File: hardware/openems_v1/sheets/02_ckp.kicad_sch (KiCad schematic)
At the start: 0 parts

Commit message: feat(hw): fecha esquemático v2 — sheets 01/02/03/05/07/11 desenhadas, ERC 0
- 01_power: nova — P-FET reverse (Q1) + F1 30A + SMBJ24CA + bulk 100µF/100nF,
  star GND (PGND/SGND/AGND) via PWR_FLAG na sheet produtora, VBAT limpo para
  o resto da placa (buck/LDO ficam no TPS65381A, sheet PMIC)
- 02_ckp / 03_cmp: CKP Hall (espelho do CMP) → MCU.PA0/PA1
- 05_analog: refeita do zero a partir do pinout_v2 (13 canais ADC), mapa
  pré-v2 descartado
- 11_mcu_h562: netlist U1 corrigido (lib_id não resolvia pinos — 100 pinos
  caíam na mesma net); globals PA0/PA1/PB4 sincronizados com as sheets acima
- 07_flex: pino corrigido para PB4 (pinout_v2)
- READMEs (hardware/openems_v1, docs/hw/schematic) actualizados ao estado
  real por sheet

Passos 1-5 do roadmap do esquemático fechados; ERC isolado por sheet em 0
erros (avisos residuais são globals sem sheet destino ainda — esperado).

Co-Authored-By: Claude Sonnet 5 <noreply@anthropic.com>
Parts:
- added C2: 330pF, Capacitor_SMD:C_0603_1608Metric, symbol Device:C
- added D2: 3V3 unidirectional, Diode_SMD:D_SOD-123, symbol Device:D_TVS
- added R10, R11: 10k, Resistor_SMD:R_0603_1608Metric, symbol Device:R
- added R12: 15k, Resistor_SMD:R_0603_1608Metric, symbol Device:R
- added R13: 330, Resistor_SMD:R_0603_1608Metric, symbol Device:R
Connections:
- new net +5V_SENS_A: R10.1
- new net AGND: C2.2, D2.2 (A2)
- new net J1.CKP_SIG: D2.1 (A1), R10.2, R11.1
- new net MCU.PA0: C2.1, R13.2
- new net N_CKP_DIV: R11.2, R12.1, R13.1
- new net SGND: R12.2
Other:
- note added: "Sheet 02 — CKP Hall (60-2) → MCU.PA0 | mirror of 03_cmp"

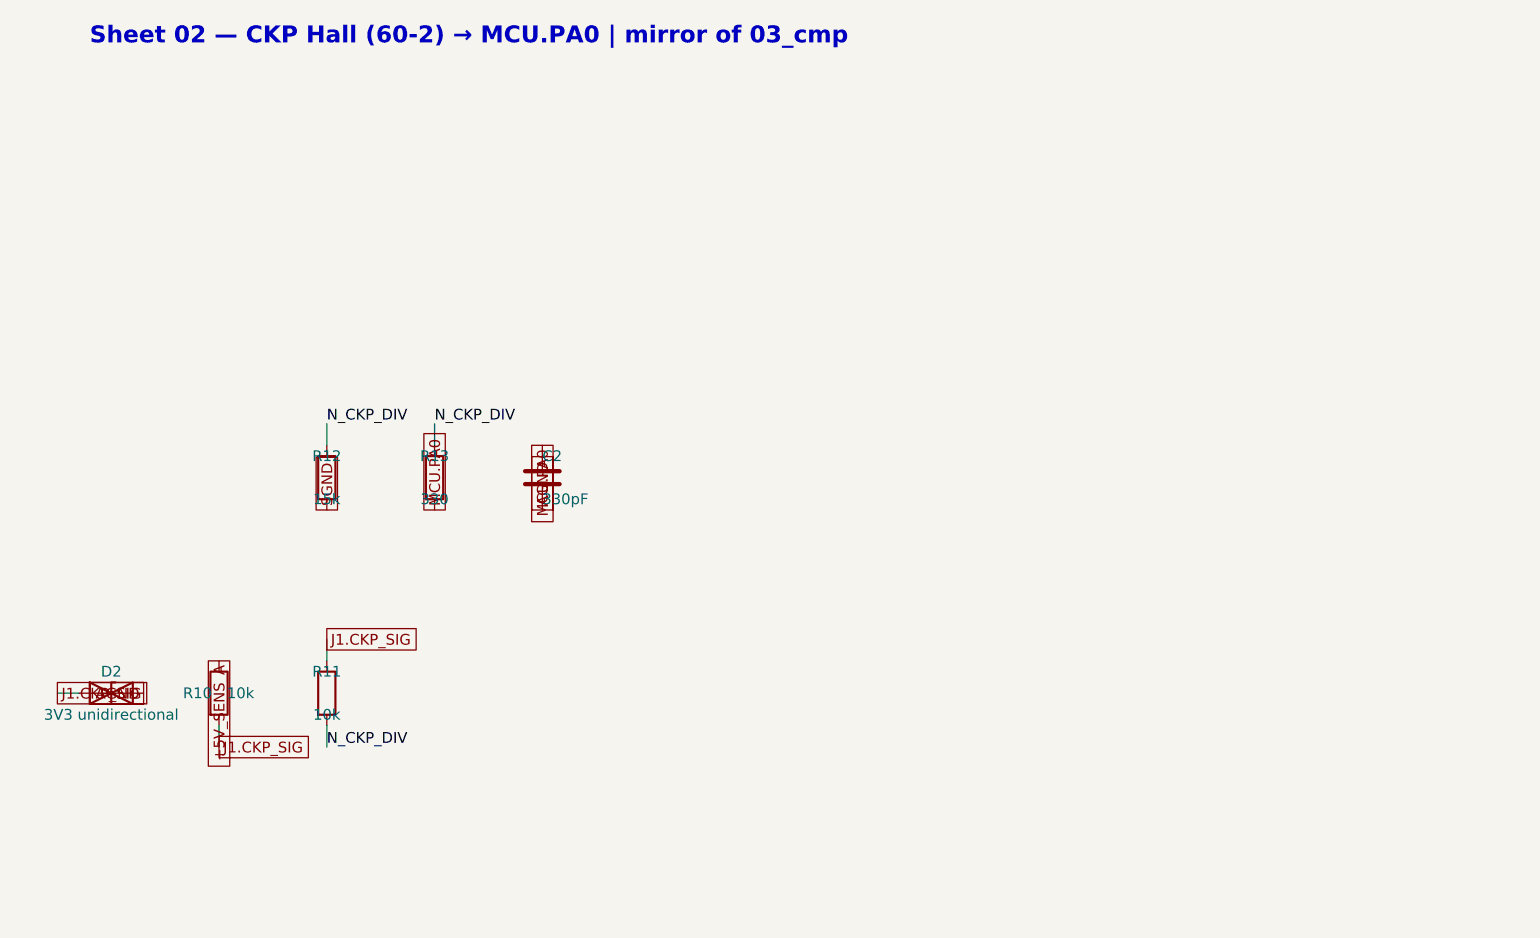
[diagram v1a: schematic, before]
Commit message: fix(hw): corrige legibilidade de 01_power e 02_ckp — layout, não topologia
Render visual (kicad-cli export svg) mostrou os componentes sobrepostos uns
aos outros (D1/C1/C2 e R10/D2 amontoados no canto da folha) apesar do ERC
0 erros — ERC não valida legibilidade, só conectividade. Nenhum bloco
tinha sido efectivamente olhado desde que foi desenhado.

- Pitch entre componentes alargado (10-15mm → 20-35mm)
- Valores do Value field encurtados (o detalhe fica na doc, não no canvas)
- Orientação dos labels ajustada para apontar para fora do corpo do
  símbolo em vez de atravessá-lo (Q1 gate, D1/D2 TVS, C2)
- Conectividade eléctrica idêntica à anterior — só reposicionamento;
  ERC 0 erros mantido nas duas sheets

Co-Authored-By: Claude Sonnet 5 <noreply@anthropic.com>
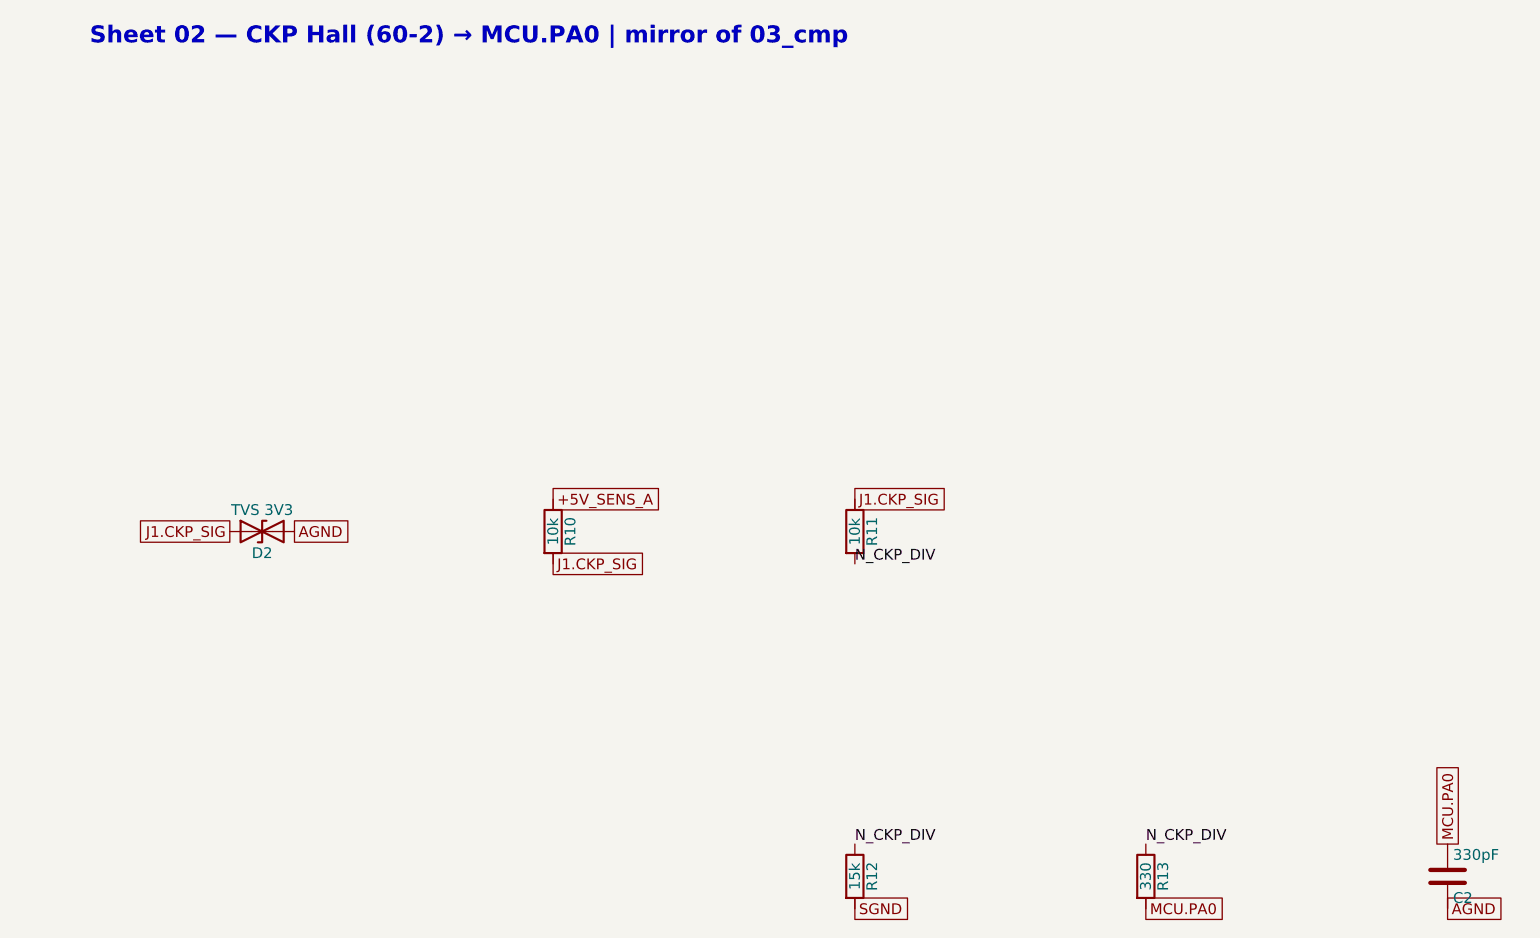
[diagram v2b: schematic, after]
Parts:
- D2: value 3V3 unidirectional -> TVS 3V3
